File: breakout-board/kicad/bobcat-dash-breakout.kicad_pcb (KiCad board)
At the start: 2 copper layers, 162 x 134 mm, 152 parts, among them J1 TO PI (40-pin ribbon), J10 ADS1115, J11 LIGHTS, J12 COIL, J13 TILT, J14 TEMP PROBE, J2 POWER IN, J3 TO 5V BUCK, J4 SWITCHES, J5 TACH, J6 FUEL, J7 HORN, J8 SILENCE, J9 MAX98357A, Q1 IRLZ44N, Q2 IRF4905, Q3 BC547B, Q4 BC547B, U1 PC817, U10 PC817, U11 DS18B20, U4 PC817, U5 PC817, U6 CD4060BE, U7 PC817, U8 PC817, U9 PC817

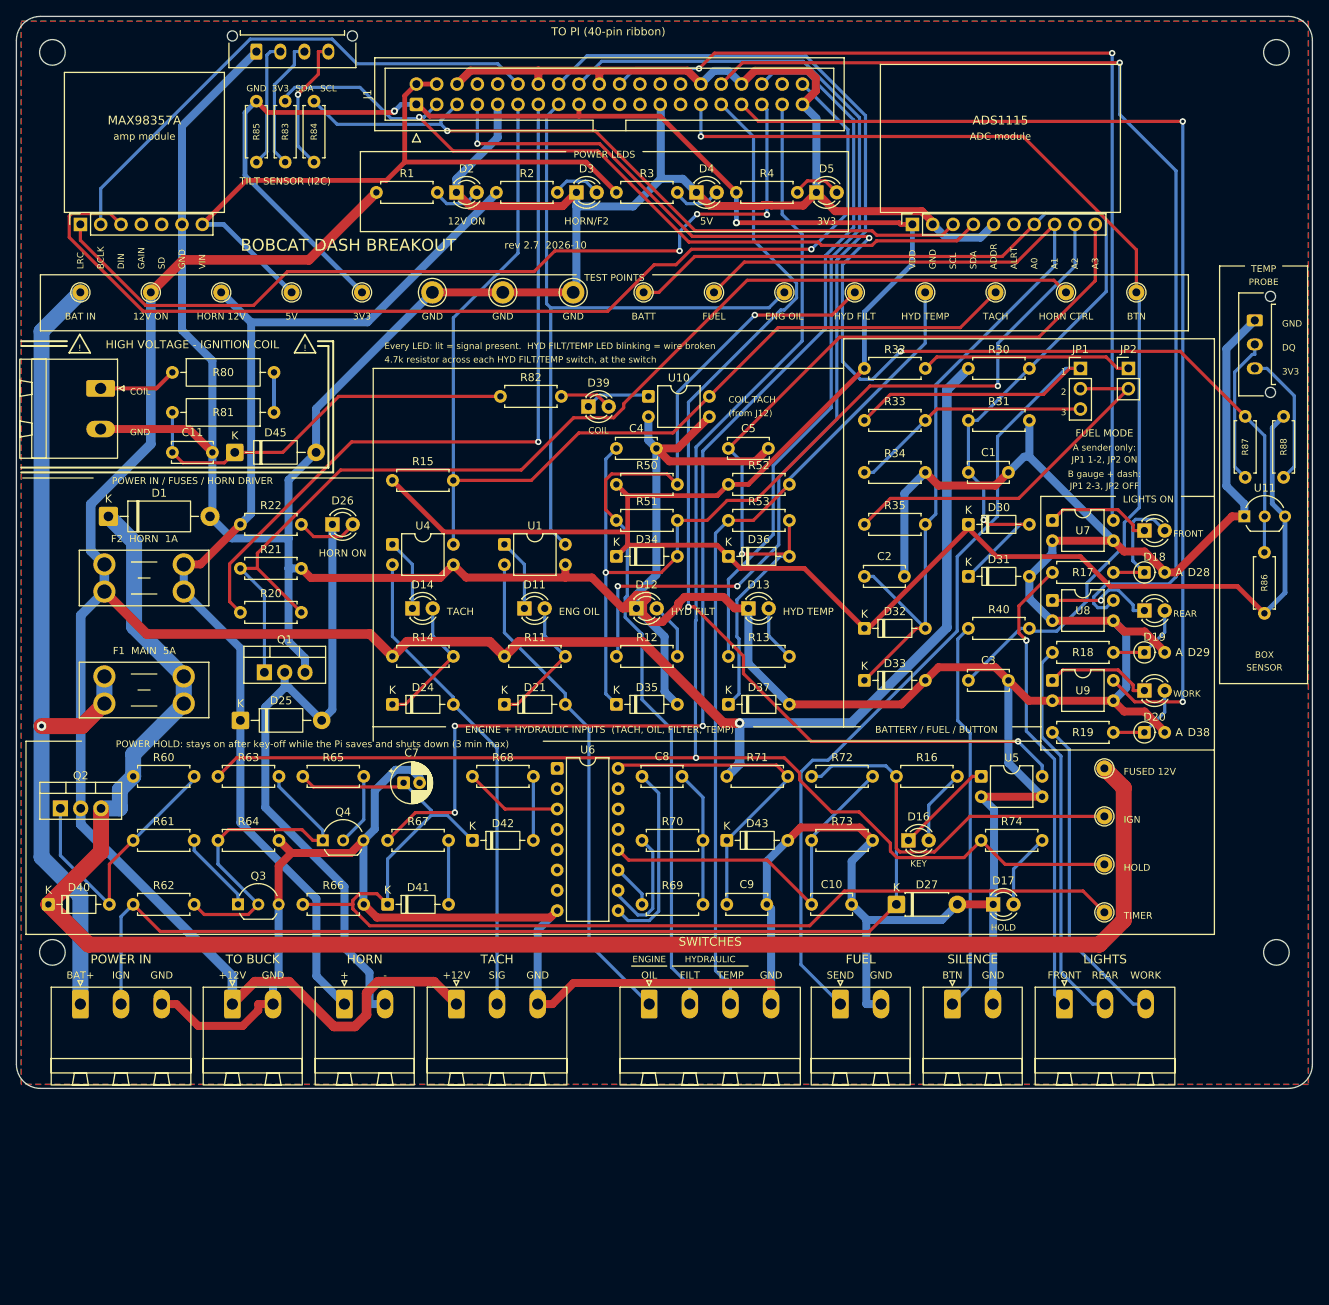
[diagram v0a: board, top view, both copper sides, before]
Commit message: Board rev 2.8: two-row ADS1115, mono/stereo amp sites, 162 x 159 mm; ADS1115 adapter
Breakout board rev 2.8:
- ADS1115 (Adafruit 1085, STEMMA QT) plugs straight in: J10 + J15, two 6-pin
  rows 12.7 mm apart, with M2.5 standoff holes H5-H8
- Amp: mono board (Adafruit 3006) on J9 with standoff holes H9-H10, or the
  stereo board (Adafruit 6513) on new J16 with corner holes H11-H14. Same
  I2S signals, fit one only
- Board 25 mm taller (162 x 159 mm): new top strip for the stereo site, the
  title and the Project Moon Pi logo (now on top). Top mounting holes moved:
  153 x 137.5 mm; drilling template updated
- Freerouting output logged to out/route.log (headless: its GUI mode never
  saves the result)

New ADS1115 adapter board (breakout-board/adapter): lets a 10-pin inline
ADS1115 (older Adafruit / clones) plug into the two-row socket, straight-
through wiring, same standoffs, logo top and back. Own generator and build.

Co-Authored-By: Claude Opus 5.5 <noreply@anthropic.com>
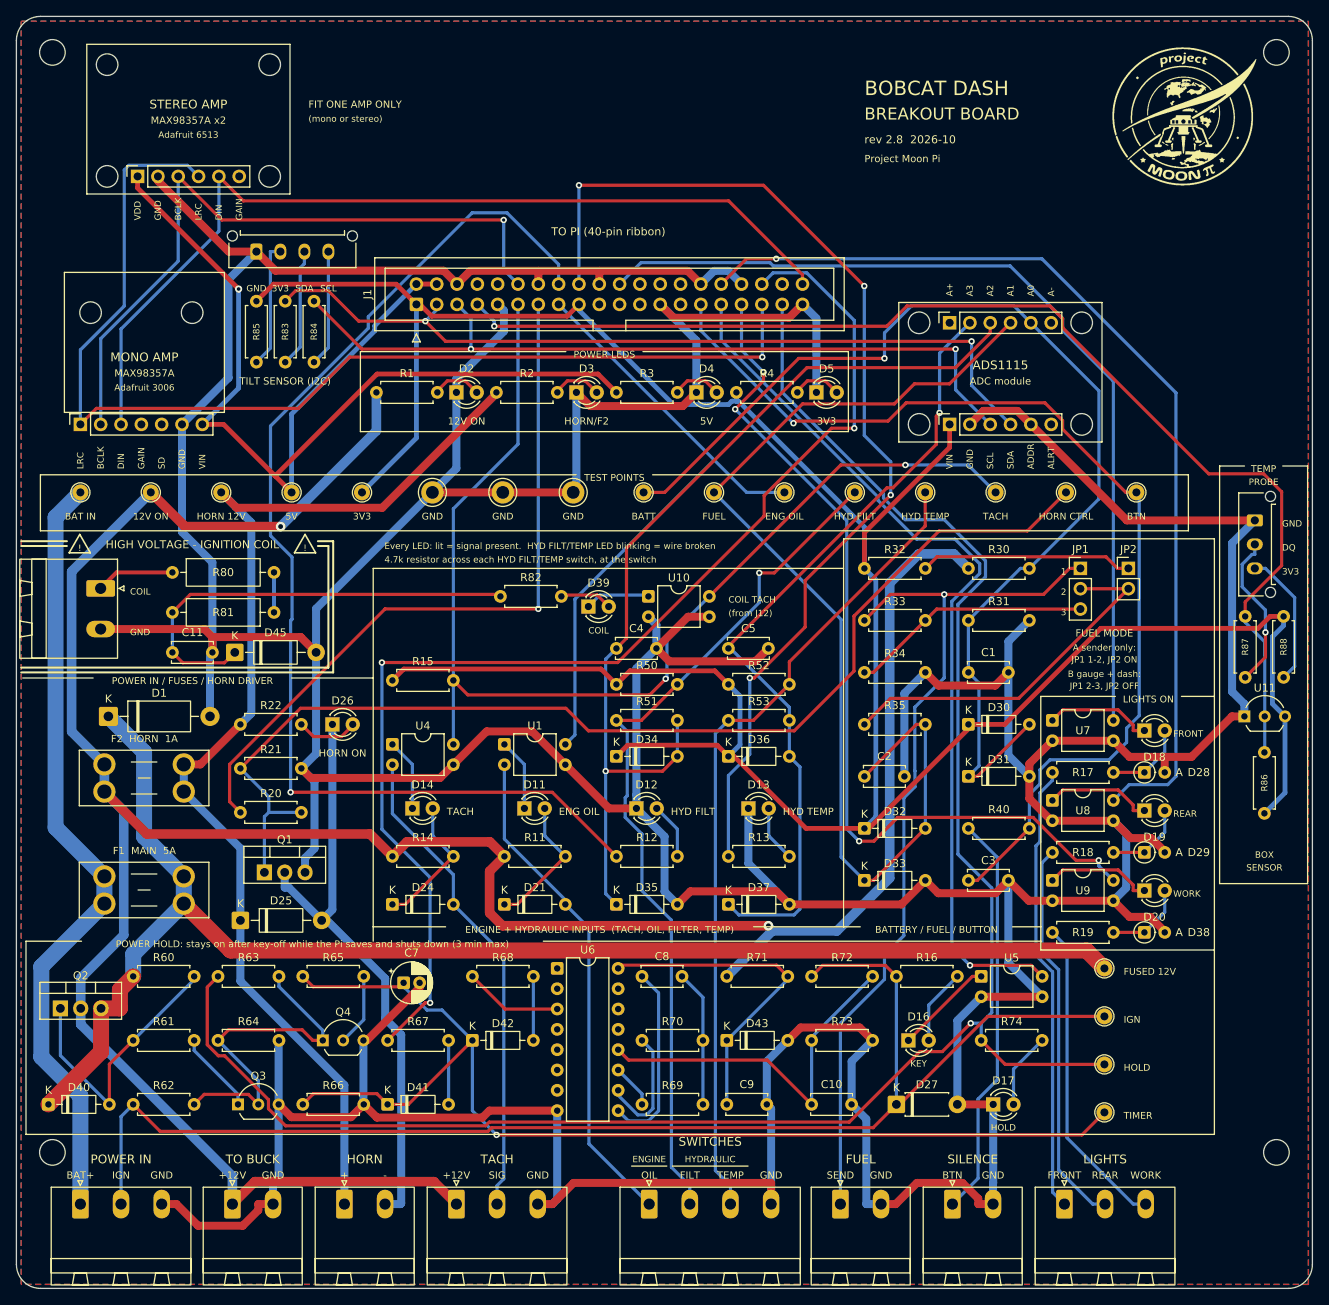
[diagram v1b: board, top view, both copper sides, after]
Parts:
- added H10: M2.5, MountingHole:MountingHole_2.7mm_M2.5, F.Cu at (22.0, 37.0)
- added H11: M2.5, MountingHole:MountingHole_2.7mm_M2.5, F.Cu at (11.3, 20.0)
- added H12: M2.5, MountingHole:MountingHole_2.7mm_M2.5, F.Cu at (31.7, 20.0)
- added H13: M2.5, MountingHole:MountingHole_2.7mm_M2.5, F.Cu at (11.3, 6.03)
- added H14: M2.5, MountingHole:MountingHole_2.7mm_M2.5, F.Cu at (31.7, 6.03)
- added H5: M2.5, MountingHole:MountingHole_2.7mm_M2.5, F.Cu at (112.8, 38.3)
- added H6: M2.5, MountingHole:MountingHole_2.7mm_M2.5, F.Cu at (133.2, 38.3)
- added H7: M2.5, MountingHole:MountingHole_2.7mm_M2.5, F.Cu at (112.8, 51.0)
- added H8: M2.5, MountingHole:MountingHole_2.7mm_M2.5, F.Cu at (133.2, 51.0)
- added H9: M2.5, MountingHole:MountingHole_2.7mm_M2.5, F.Cu at (9.27, 37.0)
- added J15: ADS1115 INPUTS, Connector_PinSocket_2.54mm:PinSocket_1x06_P2.54mm_Vertical, F.Cu at (116.7, 38.3)
- added J16: MAX98357A STEREO, Connector_PinSocket_2.54mm:PinSocket_1x06_P2.54mm_Vertical, F.Cu at (15.2, 20.0)
- J10: value ADS1115 -> ADS1115 PWR/I2C; footprint Connector_PinSocket_2.54mm:PinSocket_1x10_P2.54mm_Vertical -> Connector_PinSocket_2.54mm:PinSocket_1x06_P2.54mm_Vertical
- J9: value MAX98357A -> MAX98357A MONO
- moved J10 25.4 mm to (116.7, 51.0)
- moved J11 25.0 mm to (131.0, 148.5)
- moved J2 25.0 mm to (8.00, 148.5)
- moved J3 25.0 mm to (27.0, 148.5)
- moved J4 25.0 mm to (79.1, 148.5)
- moved J5 25.0 mm to (55.0, 148.5)
- moved J6 25.0 mm to (103.0, 148.5)
- moved J7 25.0 mm to (41.0, 148.5)
- moved J8 25.0 mm to (117.0, 148.5)
- moved C1 25.0 mm to (119.0, 82.0)
- moved C10 25.0 mm to (99.4, 136.0)
- moved C11 25.0 mm to (19.5, 79.5)
- moved C2 25.0 mm to (106.0, 95.0)
- moved C3 25.0 mm to (119.0, 108.0)
- moved C4 25.0 mm to (75.0, 79.0)
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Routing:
- net +5V: track 84.1 -> 136.7 mm, vias 0 -> 1
- net GND: track 951.9 -> 999.4 mm
- net +12V_BAT: track 218.5 -> 179.2 mm
- net HOLD_GPIO: track 208.4 -> 241.8 mm
- net I2S_LRC: track 111.4 -> 139.5 mm, vias 3 -> 1
- net LT_WORK_GPIO: track 138.4 -> 112.8 mm, vias 2 -> 4
- net TEMP_LED: track 113.3 -> 134.6 mm, vias 0 -> 4
- net I2S_BCLK: track 66.7 -> 86.7 mm, vias 0 -> 1
- net I2S_DIN: track 134.5 -> 115.3 mm, vias 1 -> 0
- net +3V3: track 343.3 -> 361.6 mm, vias 2 -> 0
- net KEY_GPIO: track 127.7 -> 110.8 mm, vias 2 -> 1
- net +12V: track 332.7 -> 349.4 mm, vias 1 -> 2
- net /FUEL_IN: track 127.9 -> 111.3 mm, vias 0 -> 1
- net BATT_ADC: track 124.6 -> 139.9 mm
- net FILT_LED: track 132.2 -> 144.0 mm, vias 2 -> 1
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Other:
- board size 162 x 134 mm -> 162 x 159 mm
- board text added: "(mono or stereo)"
- board text added: "A+"
- board text added: "A-"
- board text added: "Adafruit 3006"
- board text added: "Adafruit 6513"
- board text added: "BOBCAT DASH"
- board text added: "BREAKOUT BOARD"
- board text added: "FIT ONE AMP ONLY"
- board text added: "MAX98357A x2"
- board text added: "MONO AMP"
- board text added: "Project Moon Pi"
- board text added: "STEREO AMP"
- board text added: "rev 2.8 2026-10"
- board text removed: "BOBCAT DASH BREAKOUT"
- board text removed: "amp module"
- board text removed: "rev 2.7 2026-10"

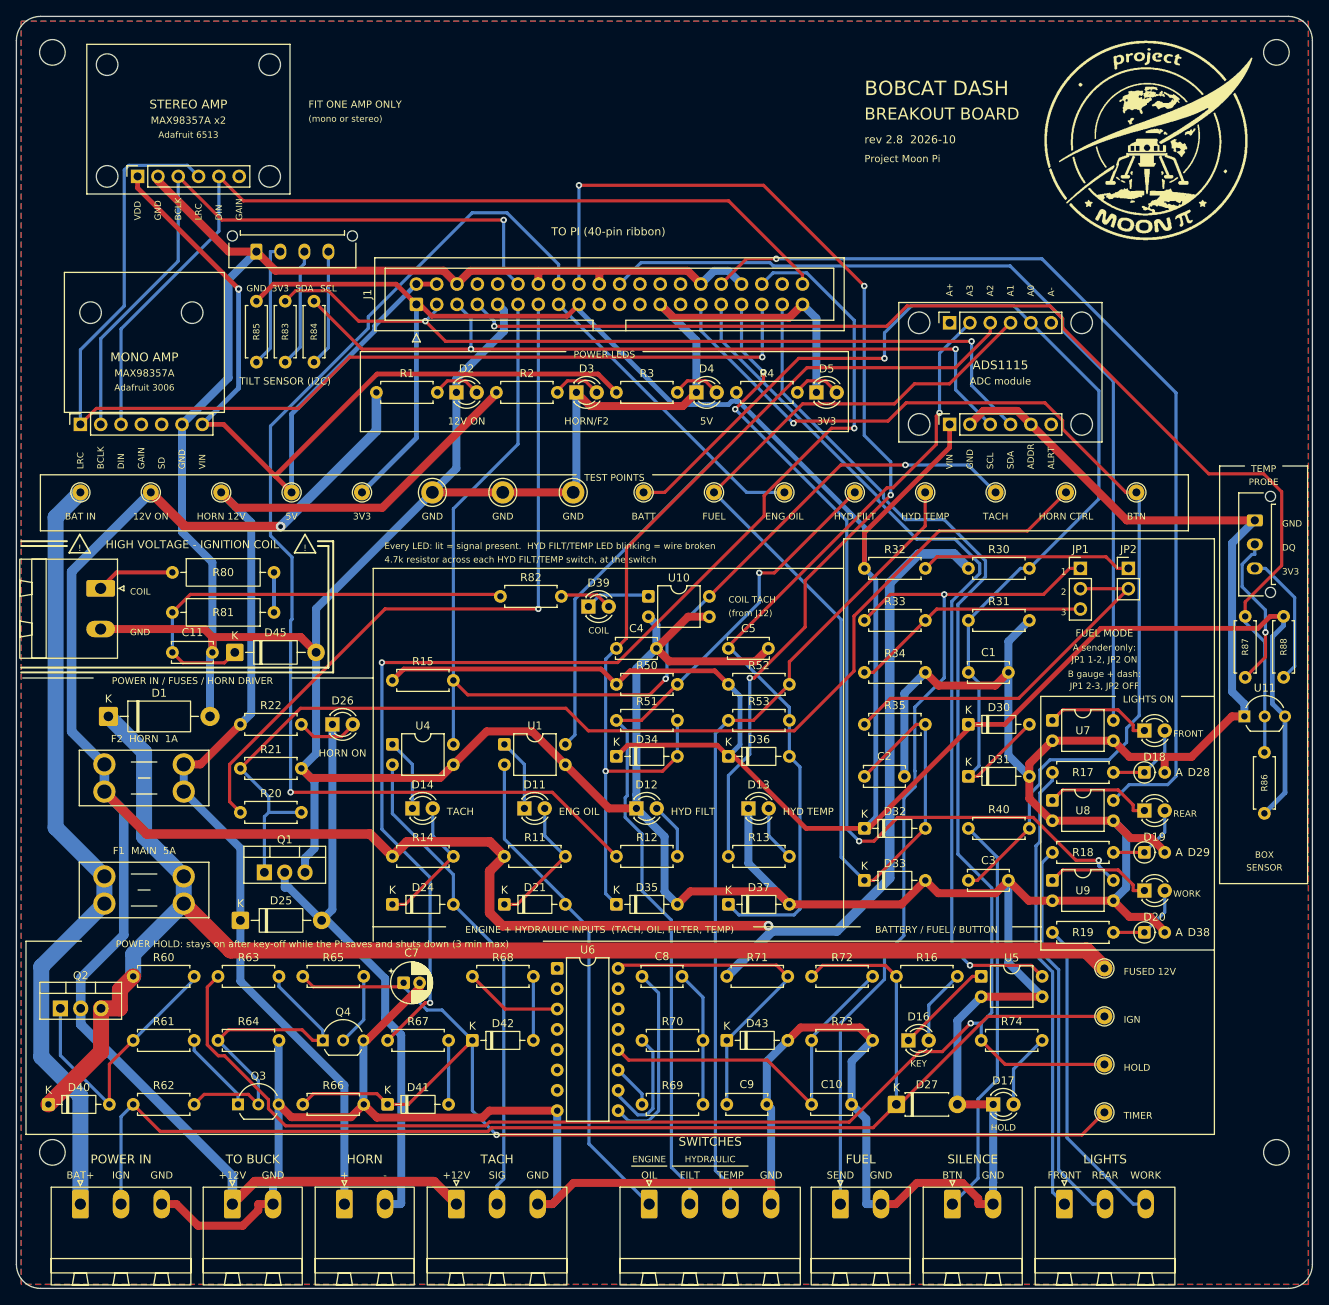
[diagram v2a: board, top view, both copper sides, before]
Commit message: Board rev 2.8 re-layout: ribbon header on the top edge, amps side by side, 9 mounting holes, standoff keepouts
- Pi ribbon header J1 and the power LEDs move to the top edge (ribbon goes
  straight up to the lid); TILT plug to the top-left corner
- Stereo amp site J16 now sits beside the mono amp J9 ("fit one amp only")
- 9 M3 mounting holes against vibration: corners, mid-sides (H15-H18) and
  one near the centre (H19); drilling template updated
- Copper-free rings around every hole on both sides (M3 r 4 mm, M2.5 r 3 mm,
  extended to nearby edges): brass standoffs need no insulating washers and
  never tie board ground to the box
- ADS1115 adapter: same standoff keepouts
- README, parts list and BOM spreadsheet updated (9 M3 standoffs, brass notes)

Co-Authored-By: Claude Opus 5.5 <noreply@anthropic.com>
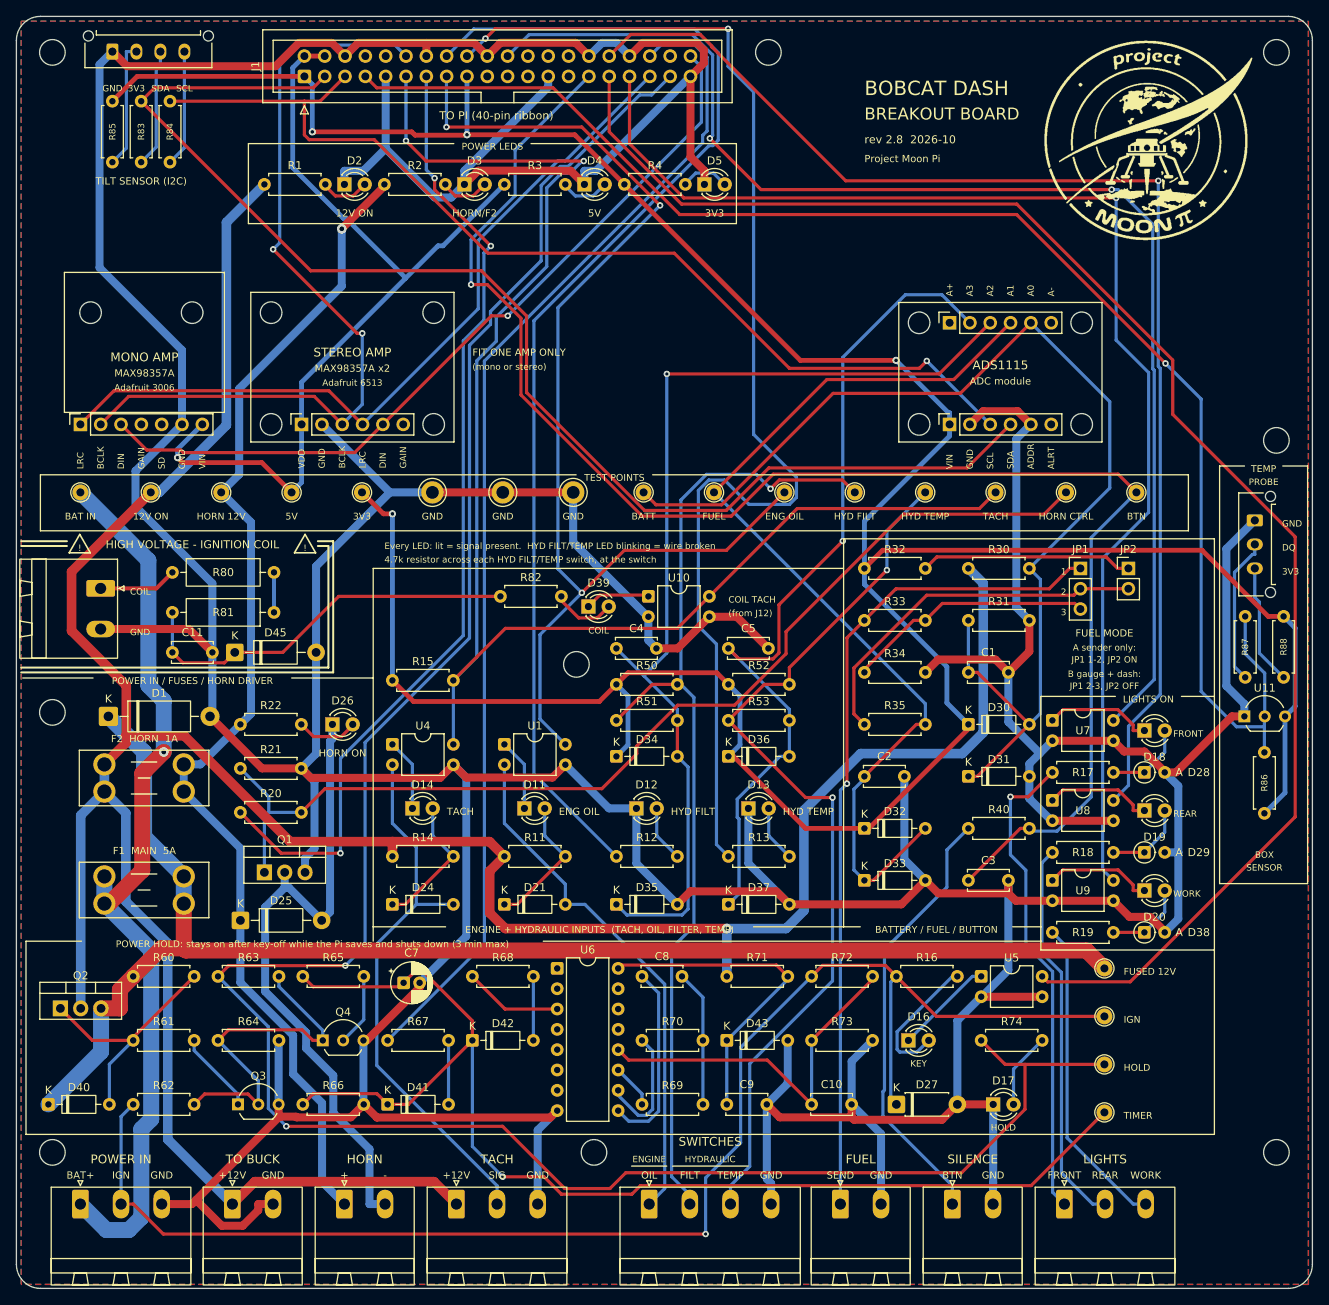
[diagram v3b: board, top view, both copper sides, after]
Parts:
- added H15: M3, MountingHole:MountingHole_3.2mm_M3, F.Cu at (94.0, 4.50)
- added H16: M3, MountingHole:MountingHole_3.2mm_M3, F.Cu at (72.2, 142.0)
- added H17: M3, MountingHole:MountingHole_3.2mm_M3, F.Cu at (4.50, 87.0)
- added H18: M3, MountingHole:MountingHole_3.2mm_M3, F.Cu at (157.5, 53.0)
- added H19: M3, MountingHole:MountingHole_3.2mm_M3, F.Cu at (70.0, 81.0)
- moved H11 37.2 mm to (31.8, 51.0)
- moved H13 37.2 mm to (31.8, 37.0)
- moved J16 37.2 mm to (35.6, 51.0)
- moved H12 37.2 mm to (52.2, 51.0)
- moved H14 37.2 mm to (52.2, 37.0)
- moved J1 31.8 mm to (36.0, 7.50)
- moved J13 30.8 mm to (12.0, 4.40)
- moved R83 30.8 mm to (15.6, 10.6)
- moved R84 30.8 mm to (19.2, 10.6)
- moved R85 30.8 mm to (12.0, 10.6)
- moved D2 29.5 mm to (41.0, 21.0)
- moved D3 29.5 mm to (56.0, 21.0)
- moved D4 29.5 mm to (71.0, 21.0)
- moved D5 29.5 mm to (86.0, 21.0)
- moved R1 29.5 mm to (31.0, 21.0)
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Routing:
- net KEY_GPIO: track 110.8 -> 193.1 mm, vias 1 -> 0
- net BTN_GPIO: track 131.3 -> 196.4 mm
- net OIL_GPIO: track 81.2 -> 145.0 mm, vias 0 -> 3
- net SDA: track 104.0 -> 164.1 mm, vias 2 -> 0
- net LT_FRONT_GPIO: track 112.3 -> 162.4 mm, vias 0 -> 2
- net LT_WORK_GPIO: track 112.8 -> 162.0 mm, vias 4 -> 1
- net HOLD_GPIO: track 241.8 -> 290.1 mm, vias 1 -> 2
- net TACH_GPIO: track 143.0 -> 189.3 mm
- net I2S_LRC: track 139.5 -> 97.7 mm, vias 1 -> 0
- net W1_DQ: track 148.9 -> 185.5 mm
- net +3V3: track 361.6 -> 397.3 mm, vias 0 -> 4
- net LT_REAR_GPIO: track 122.1 -> 157.4 mm
- net HORN_GPIO: track 91.3 -> 122.9 mm, vias 1 -> 3
- net SCL: track 100.2 -> 128.9 mm, vias 2 -> 1
- net +5V: track 136.7 -> 108.3 mm
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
